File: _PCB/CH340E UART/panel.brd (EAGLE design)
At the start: 21.1 x 11.4 mm, 11 parts, among them IC1 REG1117

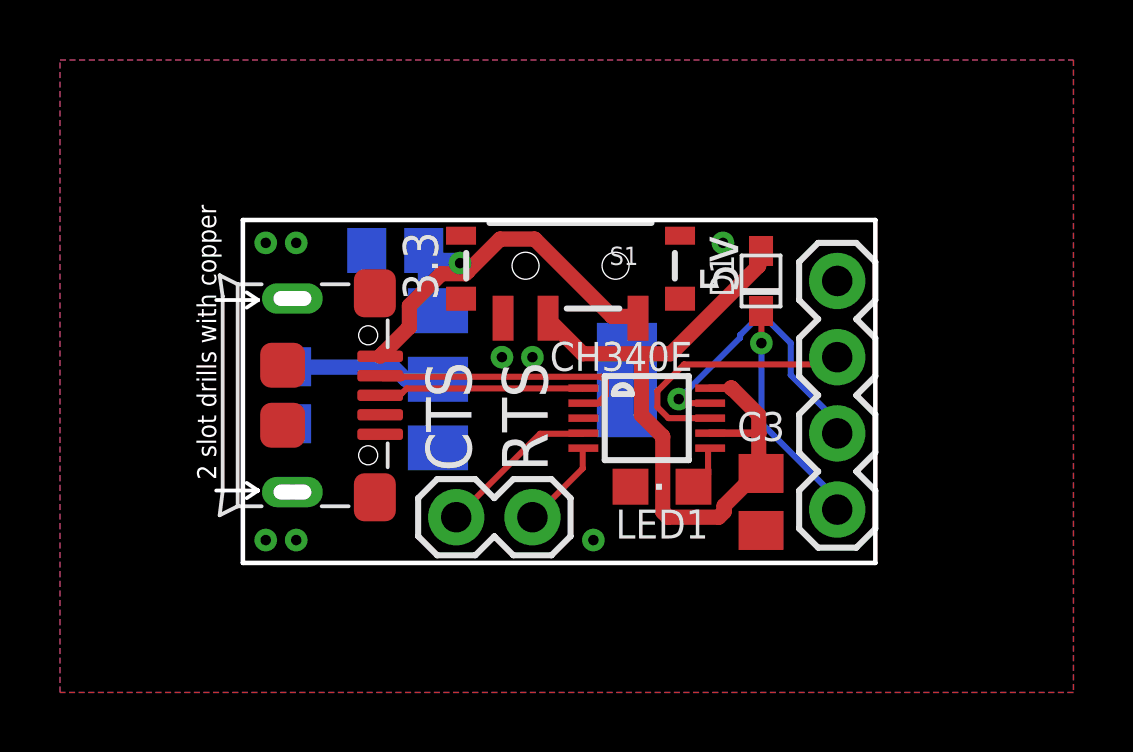
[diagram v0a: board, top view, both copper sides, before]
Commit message: CH340E converter complete + LoRa sensor node
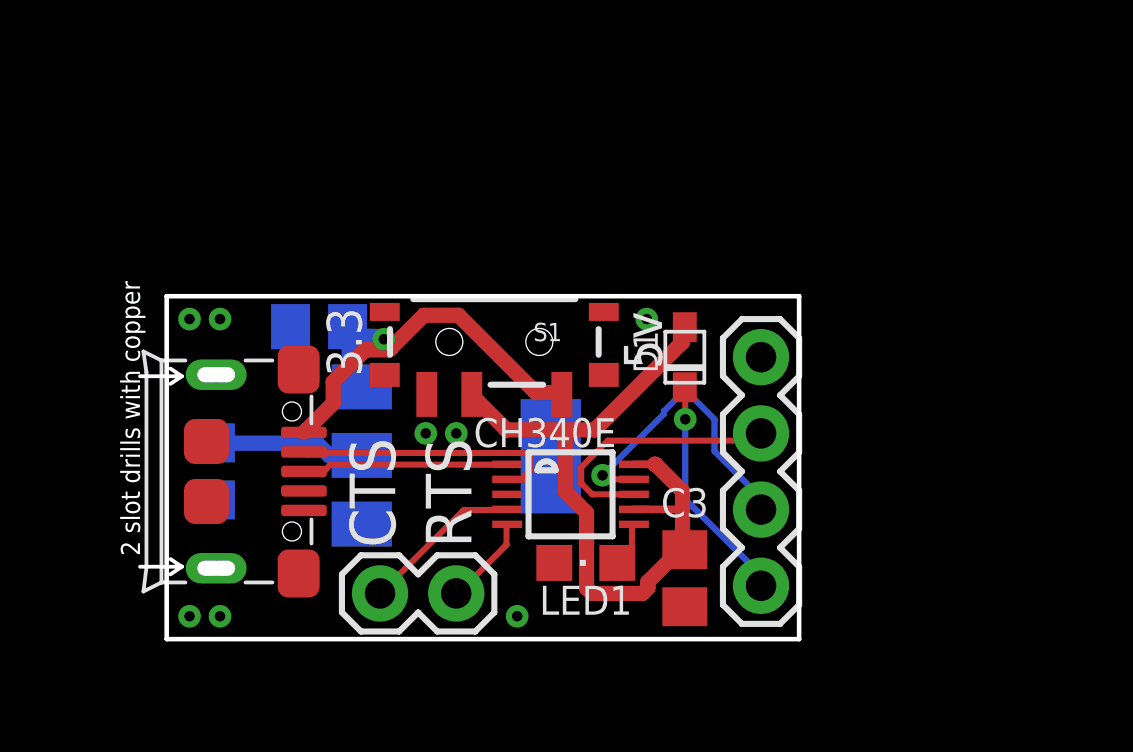
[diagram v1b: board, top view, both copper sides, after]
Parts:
- moved D1 3.59 mm to (17.3, 9.40)
- moved C3 3.59 mm to (17.3, 2.03)
- moved C1 3.59 mm to (5.08, 10.4)
- moved J2 3.59 mm to (9.65, 1.52)
- moved LED1 3.59 mm to (14.0, 2.54)
- moved C2 3.59 mm to (1.52, 5.59)
- moved USB2 3.59 mm to (4.83, 5.59)
- moved CH340E 3.59 mm to (13.5, 4.83)
- moved IC1 3.59 mm to (9.65, 6.10)
- moved J1 3.59 mm to (19.8, 1.78)
- moved S1 3.59 mm to (10.9, 9.91)
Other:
- board text added: "C1"
- board text added: "C2"
- board text added: "C3"
- board text added: "CH340E"
- board text added: "D1"
- board text added: "LED1"
- board text added: "S1"

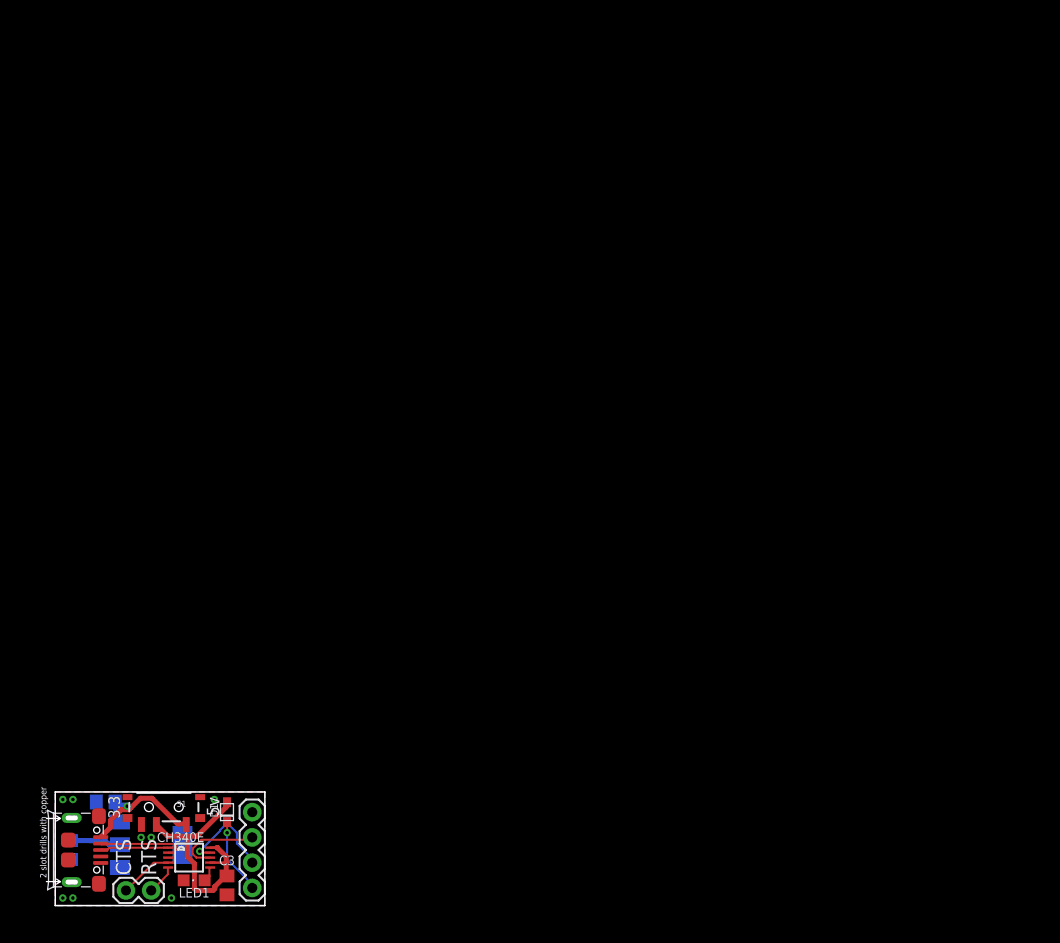
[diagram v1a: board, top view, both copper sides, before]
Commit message: CH340E board panelized
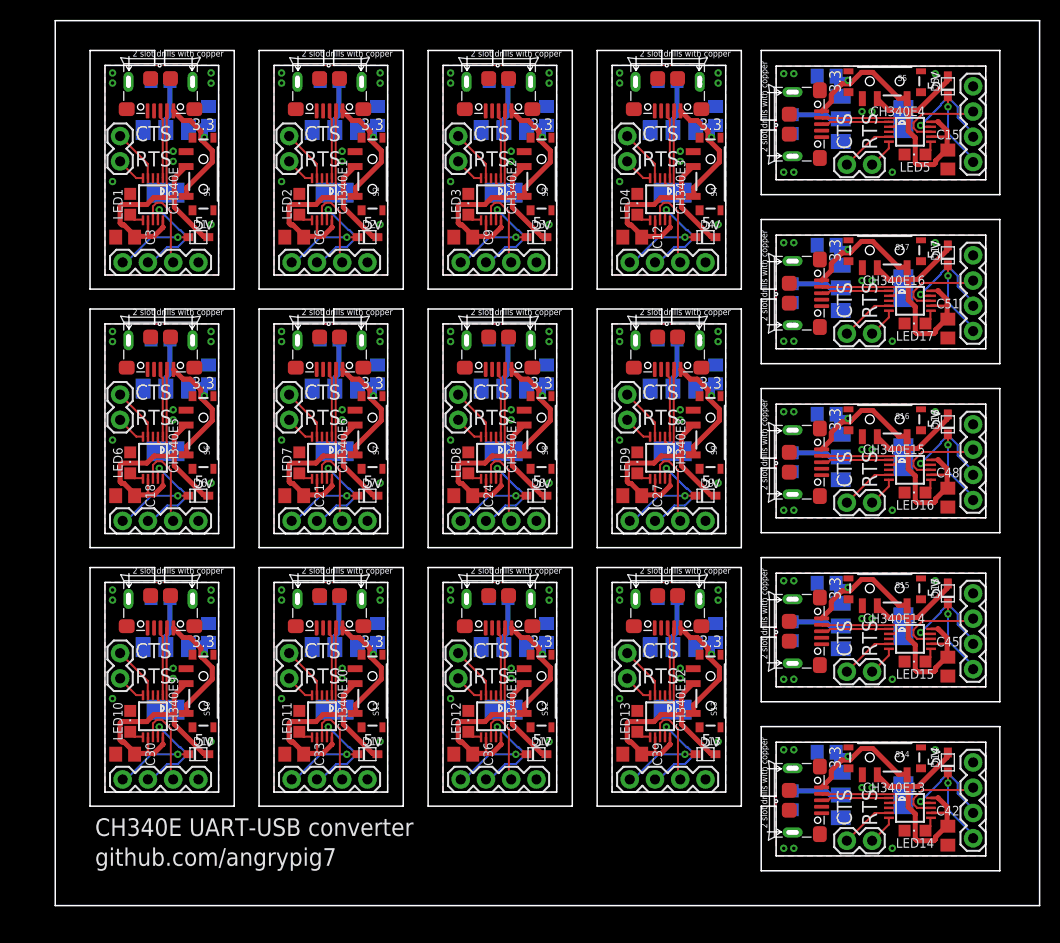
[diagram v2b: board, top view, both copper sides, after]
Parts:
- added C10, C11, C12, C13, C14, C15, C16, C17, C18, C19, C20, C21, C22, C23, C24, C25, C26, C27, C28, C29, C30, C31, C32, C33, C34, C35, C36, C37, C38, C39, C4, C40, C41, C42, C43, C44, C45, C46, C47, C48, C49, C5, C50, C51, C6, C7, C8, C9: 100nF, rcl-2:C0805
- added CH340E1, CH340E10, CH340E11, CH340E12, CH340E13, CH340E14, CH340E15, CH340E16, CH340E2, CH340E3, CH340E4, CH340E5, CH340E6, CH340E7, CH340E8, CH340E9: CH340ESMD, CH340E:MSOP10
- added D10, D11, D12, D13, D14, D15, D16, D17, D2, D3, D4, D5, D6, D7, D8, D9: (no value), adafruit:SOD-323F
- added IC10, IC11, IC12, IC13, IC14, IC15, IC16, IC17, IC2, IC3, IC4, IC5, IC6, IC7, IC8, IC9: REG1117, burr-brown-3:SOT223
- added J10, J12, J14, J16, J18, J20, J22, J24, J26, J28, J30, J32, J34, J4, J6, J8: (no value), SparkFun-Connectors:1X02
- added J11, J13, J15, J17, J19, J21, J23, J25, J27, J29, J3, J31, J33, J5, J7, J9: (no value), SparkFun-Connectors:1X04
- added LED10, LED11, LED12, LED13, LED14, LED15, LED16, LED17, LED2, LED3, LED4, LED5, LED6, LED7, LED8, LED9: (no value), adafruit:CHIPLED_0805
- added S10, S11, S12, S13, S14, S15, S16, S17, S2, S3, S4, S5, S6, S7, S8, S9: (no value), SparkFun-Switches:SWITCH_SPST_SMD_A
- added USB1, USB10, USB11, USB12, USB13, USB14, USB15, USB16, USB17, USB3, USB4, USB5, USB6, USB7, USB8, USB9: ST-USB-001G, Seeed-Connector:MICRO-USB5+4P-SMD-0.65-B
- moved C2 77.9 mm to (10.6, 83.0), turned to 0 degrees
- moved USB2 74.3 mm to (10.6, 79.7), turned to 180 degrees
- moved J2 73.4 mm to (6.52, 74.8), turned to 90 degrees
- moved C1 69.8 mm to (15.4, 79.4), turned to 90 degrees
- moved IC1 68.8 mm to (11.1, 74.8), turned to 180 degrees
- moved LED1 68.3 mm to (7.54, 70.5), turned to 0 degrees
- moved CH340E 66.3 mm to (9.83, 71.0), turned to 270 degrees
- moved C3 66.0 mm to (7.03, 67.2), turned to 180 degrees
- moved J1 64.2 mm to (6.78, 64.7), turned to 0 degrees
- moved S1 63.8 mm to (14.9, 73.6), turned to 270 degrees
- moved D1 57.9 mm to (14.4, 67.2), turned to 180 degrees
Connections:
- new net 3.3V1: S2.1
- new net 3.3V10: S11.1
- new net 3.3V11: S12.1
- new net 3.3V12: S13.1
- new net 3.3V13: S14.1
- new net 3.3V14: S15.1
- new net 3.3V15: S16.1
- new net 3.3V16: S17.1
- new net 3.3V2: S3.1
- new net 3.3V3: S4.1
- new net 3.3V4: S5.1
- new net 3.3V5: S6.1
- new net 3.3V6: S7.1
- new net 3.3V7: S8.1
- new net 3.3V8: S9.1
- new net 3.3V9: S10.1
- new net 3V1: C5.1, IC2.2
- new net 3V10: C29.1, IC10.2
- new net 3V11: C32.1, IC11.2
- new net 3V12: C35.1, IC12.2
- new net 3V13: C38.1, IC13.2
- new net 3V14: C41.1, IC14.2
- new net 3V15: C44.1, IC15.2
- new net 3V16: C47.1, IC16.2
- new net 3V17: C50.1, IC17.2
- new net 3V2: C8.1, IC3.2
- new net 3V4: C11.1, IC4.2
- new net 3V5: C14.1, IC5.2
- new net 3V6: C17.1, IC6.2
- new net 3V7: C20.1, IC7.2
- new net 3V8: C23.1, IC8.2
- new net 3V9: C26.1, IC9.2
- new net 5V1: C4.1, IC2.3, S2.3, USB1.1
- new net 5V10: C31.1, IC11.3, S11.3, USB11.1
- new net 5V11: C34.1, IC12.3, S12.3, USB12.1
- new net 5V12: C37.1, IC13.3, S13.3, USB13.1
- new net 5V13: C40.1, IC14.3, S14.3, USB14.1
- new net 5V14: C43.1, IC15.3, S15.3, USB15.1
- new net 5V15: C46.1, IC16.3, S16.3, USB16.1
- new net 5V16: C49.1, IC17.3, S17.3, USB17.1
- new net 5V2: C7.1, IC3.3, S3.3, USB3.1
- new net 5V3: C10.1, IC4.3, S4.3, USB4.1
- new net 5V4: C13.1, IC5.3, S5.3, USB5.1
- new net 5V5: C16.1, IC6.3, S6.3, USB6.1
- new net 5V6: C19.1, IC7.3, S7.3, USB7.1
- new net 5V7: C22.1, IC8.3, S8.3, USB8.1
- new net 5V8: C25.1, IC9.3, S9.3, USB9.1
- new net 5V9: C28.1, IC10.3, S10.3, USB10.1
- new net CTS1: CH340E1.5, J4.1
- new net CTS10: CH340E10.5, J22.1
- new net CTS11: CH340E11.5, J24.1
- new net CTS12: CH340E12.5, J26.1
- new net CTS13: CH340E13.5, J28.1
- new net CTS14: CH340E14.5, J30.1
- new net CTS15: CH340E15.5, J32.1
- new net CTS16: CH340E16.5, J34.1
- new net CTS2: CH340E2.5, J6.1
- new net CTS3: CH340E3.5, J8.1
- new net CTS4: CH340E4.5, J10.1
- new net CTS5: CH340E5.5, J12.1
- new net CTS6: CH340E6.5, J14.1
- new net CTS7: CH340E7.5, J16.1
- new net CTS8: CH340E8.5, J18.1
- new net CTS9: CH340E9.5, J20.1
- new net GND1: C4.2, C5.2, C6.2, CH340E1.3, IC2.1, J3.4, LED2.C, USB1.5, USB1.S1, USB1.S2, USB1.S3, USB1.S4, USB1.S5, USB1.S6
- new net GND10: C31.2, C32.2, C33.2, CH340E10.3, IC11.1, J21.4, LED11.C, USB11.5, USB11.S1, USB11.S2, USB11.S3, USB11.S4, USB11.S5, USB11.S6
- new net GND11: C34.2, C35.2, C36.2, CH340E11.3, IC12.1, J23.4, LED12.C, USB12.5, USB12.S1, USB12.S2, USB12.S3, USB12.S4, USB12.S5, USB12.S6
- new net GND12: C37.2, C38.2, C39.2, CH340E12.3, IC13.1, J25.4, LED13.C, USB13.5, USB13.S1, USB13.S2, USB13.S3, USB13.S4, USB13.S5, USB13.S6
- new net GND13: C40.2, C41.2, C42.2, CH340E13.3, IC14.1, J27.4, LED14.C, USB14.5, USB14.S1, USB14.S2, USB14.S3, USB14.S4, USB14.S5, USB14.S6
- new net GND14: C43.2, C44.2, C45.2, CH340E14.3, IC15.1, J29.4, LED15.C, USB15.5, USB15.S1, USB15.S2, USB15.S3, USB15.S4, USB15.S5, USB15.S6
- new net GND15: C46.2, C47.2, C48.2, CH340E15.3, IC16.1, J31.4, LED16.C, USB16.5, USB16.S1, USB16.S2, USB16.S3, USB16.S4, USB16.S5, USB16.S6
- new net GND16: C49.2, C50.2, C51.2, CH340E16.3, IC17.1, J33.4, LED17.C, USB17.5, USB17.S1, USB17.S2, USB17.S3, USB17.S4, USB17.S5, USB17.S6
- new net GND2: C7.2, C8.2, C9.2, CH340E2.3, IC3.1, J5.4, LED3.C, USB3.5, USB3.S1, USB3.S2, USB3.S3, USB3.S4, USB3.S5, USB3.S6
- new net GND3: C10.2, C11.2, C12.2, CH340E3.3, IC4.1, J7.4, LED4.C, USB4.5, USB4.S1, USB4.S2, USB4.S3, USB4.S4, USB4.S5, USB4.S6
- new net GND4: C13.2, C14.2, C15.2, CH340E4.3, IC5.1, J9.4, LED5.C, USB5.5, USB5.S1, USB5.S2, USB5.S3, USB5.S4, USB5.S5, USB5.S6
- new net GND5: C16.2, C17.2, C18.2, CH340E5.3, IC6.1, J11.4, LED6.C, USB6.5, USB6.S1, USB6.S2, USB6.S3, USB6.S4, USB6.S5, USB6.S6
- new net GND6: C19.2, C20.2, C21.2, CH340E6.3, IC7.1, J13.4, LED7.C, USB7.5, USB7.S1, USB7.S2, USB7.S3, USB7.S4, USB7.S5, USB7.S6
- new net GND7: C22.2, C23.2, C24.2, CH340E7.3, IC8.1, J15.4, LED8.C, USB8.5, USB8.S1, USB8.S2, USB8.S3, USB8.S4, USB8.S5, USB8.S6
- new net GND8: C25.2, C26.2, C27.2, CH340E8.3, IC9.1, J17.4, LED9.C, USB9.5, USB9.S1, USB9.S2, USB9.S3, USB9.S4, USB9.S5, USB9.S6
- new net GND9: C28.2, C29.2, C30.2, CH340E9.3, IC10.1, J19.4, LED10.C, USB10.5, USB10.S1, USB10.S2, USB10.S3, USB10.S4, USB10.S5, USB10.S6
- new net N$10: CH340E9.6, LED10.A
- new net N$11: CH340E10.6, LED11.A
- new net N$12: CH340E11.6, LED12.A
- new net N$13: CH340E12.6, LED13.A
- new net N$14: CH340E13.6, LED14.A
- new net N$15: CH340E14.6, LED15.A
- new net N$16: CH340E15.6, LED16.A
- new net N$17: CH340E16.6, LED17.A
- new net N$2: CH340E1.6, LED2.A
- new net N$3: CH340E2.6, LED3.A
- new net N$4: CH340E3.6, LED4.A
- new net N$5: CH340E4.6, LED5.A
- new net N$6: CH340E5.6, LED6.A
- new net N$7: CH340E6.6, LED7.A
- new net N$8: CH340E7.6, LED8.A
- new net N$9: CH340E8.6, LED9.A
- new net RTS1: CH340E1.4, J4.2
- new net RTS10: CH340E10.4, J22.2
- new net RTS11: CH340E11.4, J24.2
- new net RTS12: CH340E12.4, J26.2
- new net RTS13: CH340E13.4, J28.2
- new net RTS14: CH340E14.4, J30.2
- new net RTS15: CH340E15.4, J32.2
- new net RTS16: CH340E16.4, J34.2
- new net RTS2: CH340E2.4, J6.2
- new net RTS3: CH340E3.4, J8.2
- new net RTS4: CH340E4.4, J10.2
- new net RTS5: CH340E5.4, J12.2
- new net RTS6: CH340E6.4, J14.2
- new net RTS7: CH340E7.4, J16.2
- new net RTS8: CH340E8.4, J18.2
- new net RTS9: CH340E9.4, J20.2
- new net RX1: CH340E1.9, J3.2
- new net RX10: CH340E10.9, J21.2
- new net RX11: CH340E11.9, J23.2
- new net RX12: CH340E12.9, J25.2
- new net RX13: CH340E13.9, J27.2
- new net RX14: CH340E14.9, J29.2
- new net RX15: CH340E15.9, J31.2
- new net RX16: CH340E16.9, J33.2
- new net RX2: CH340E2.9, J5.2
- new net RX3: CH340E3.9, J7.2
- new net RX4: CH340E4.9, J9.2
- new net RX5: CH340E5.9, J11.2
- new net RX6: CH340E6.9, J13.2
- new net RX7: CH340E7.9, J15.2
- new net RX8: CH340E8.9, J17.2
- new net RX9: CH340E9.9, J19.2
- new net TX1: CH340E1.8, J3.3
- new net TX10: CH340E10.8, J21.3
- new net TX11: CH340E11.8, J23.3
- new net TX12: CH340E12.8, J25.3
- new net TX13: CH340E13.8, J27.3
- new net TX14: CH340E14.8, J29.3
- new net TX15: CH340E15.8, J31.3
- new net TX16: CH340E16.8, J33.3
- new net TX2: CH340E2.8, J5.3
- new net TX3: CH340E3.8, J7.3
- new net TX4: CH340E4.8, J9.3
- new net TX5: CH340E5.8, J11.3
- new net TX6: CH340E6.8, J13.3
- new net TX7: CH340E7.8, J15.3
- new net TX8: CH340E8.8, J17.3
- new net TX9: CH340E9.8, J19.3
- new net USBN1: CH340E1.2, USB1.2
- new net USBN10: CH340E10.2, USB11.2
- new net USBN11: CH340E11.2, USB12.2
- new net USBN12: CH340E12.2, USB13.2
- new net USBN13: CH340E13.2, USB14.2
- new net USBN14: CH340E14.2, USB15.2
- new net USBN15: CH340E15.2, USB16.2
- new net USBN16: CH340E16.2, USB17.2
- new net USBN2: CH340E2.2, USB3.2
- new net USBN3: CH340E3.2, USB4.2
- new net USBN4: CH340E4.2, USB5.2
- new net USBN5: CH340E5.2, USB6.2
- new net USBN6: CH340E6.2, USB7.2
- new net USBN7: CH340E7.2, USB8.2
- new net USBN8: CH340E8.2, USB9.2
- new net USBN9: CH340E9.2, USB10.2
- new net USBP1: CH340E1.1, USB1.3
- new net USBP10: CH340E10.1, USB11.3
- new net USBP11: CH340E11.1, USB12.3
- new net USBP12: CH340E12.1, USB13.3
- new net USBP13: CH340E13.1, USB14.3
- new net USBP14: CH340E14.1, USB15.3
- new net USBP15: CH340E15.1, USB16.3
- new net USBP16: CH340E16.1, USB17.3
- new net USBP2: CH340E2.1, USB3.3
- new net USBP3: CH340E3.1, USB4.3
- new net USBP4: CH340E4.1, USB5.3
- new net USBP5: CH340E5.1, USB6.3
- new net USBP6: CH340E6.1, USB7.3
- new net USBP7: CH340E7.1, USB8.3
- new net USBP8: CH340E8.1, USB9.3
- new net USBP9: CH340E9.1, USB10.3
- new net VCC1: C6.1, CH340E1.10, CH340E1.7, D2.A, S2.2
- new net VCC10: C33.1, CH340E10.10, CH340E10.7, D11.A, S11.2
- new net VCC11: C36.1, CH340E11.10, CH340E11.7, D12.A, S12.2
- new net VCC12: C39.1, CH340E12.10, CH340E12.7, D13.A, S13.2
- new net VCC13: C42.1, CH340E13.10, CH340E13.7, D14.A, S14.2
- new net VCC14: C45.1, CH340E14.10, CH340E14.7, D15.A, S15.2
- new net VCC15: C48.1, CH340E15.10, CH340E15.7, D16.A, S16.2
- new net VCC16: C51.1, CH340E16.10, CH340E16.7, D17.A, S17.2
- new net VCC2: C9.1, CH340E2.10, CH340E2.7, D3.A, S3.2
- new net VCC3: C12.1, CH340E3.10, CH340E3.7, D4.A, S4.2
- new net VCC4: C15.1, CH340E4.10, CH340E4.7, D5.A, S5.2
- new net VCC5: C18.1, CH340E5.10, CH340E5.7, D6.A, S6.2
- new net VCC6: C21.1, CH340E6.10, CH340E6.7, D7.A, S7.2
- new net VCC7: C24.1, CH340E7.10, CH340E7.7, D8.A, S8.2
- new net VCC8: C27.1, CH340E8.10, CH340E8.7, D9.A, S9.2
- new net VCC9: C30.1, CH340E9.10, CH340E9.7, D10.A, S10.2
- new net VCC_D1: D2.C, J3.1
- new net VCC_D10: D11.C, J21.1
- new net VCC_D11: D12.C, J23.1
- new net VCC_D12: D13.C, J25.1
- new net VCC_D13: D14.C, J27.1
- new net VCC_D14: D15.C, J29.1
- new net VCC_D15: D16.C, J31.1
- new net VCC_D16: D17.C, J33.1
- new net VCC_D2: D3.C, J5.1
- new net VCC_D3: D4.C, J7.1
- new net VCC_D4: D5.C, J9.1
- new net VCC_D5: D6.C, J11.1
- new net VCC_D6: D7.C, J13.1
- new net VCC_D7: D8.C, J15.1
- new net VCC_D8: D9.C, J17.1
- new net VCC_D9: D10.C, J19.1
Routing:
- net VCC16: track 0.00 -> 24.4 mm
- net VCC15: track 0.00 -> 24.4 mm
- net VCC14: track 0.00 -> 24.4 mm
- net VCC13: track 0.00 -> 24.4 mm
- net VCC4: track 0.00 -> 24.4 mm
- net VCC2: track 0.00 -> 24.4 mm
- net VCC1: track 0.00 -> 24.4 mm
- net VCC3: track 0.00 -> 24.4 mm
- net VCC11: track 0.00 -> 24.4 mm
- net VCC7: track 0.00 -> 24.4 mm
- net VCC12: track 0.00 -> 24.4 mm
- net VCC10: track 0.00 -> 24.4 mm
- net VCC9: track 0.00 -> 24.4 mm
- net VCC8: track 0.00 -> 24.4 mm
- net VCC6: track 0.00 -> 24.4 mm
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- added copper zone on layer 1, net GND1
- added copper zone on layer 16, net GND1
- added copper zone on layer 1, net GND10
- added copper zone on layer 16, net GND10
- added copper zone on layer 1, net GND11
- added copper zone on layer 16, net GND11
- added copper zone on layer 1, net GND12
- added copper zone on layer 16, net GND12
- added copper zone on layer 1, net GND13
- added copper zone on layer 16, net GND13
- added copper zone on layer 1, net GND14
- added copper zone on layer 16, net GND14
- added copper zone on layer 1, net GND15
- added copper zone on layer 16, net GND15
- added copper zone on layer 1, net GND16
- added copper zone on layer 16, net GND16
- added copper zone on layer 1, net GND2
- added copper zone on layer 16, net GND2
- added copper zone on layer 1, net GND3
- added copper zone on layer 16, net GND3
- added copper zone on layer 1, net GND4
- added copper zone on layer 16, net GND4
- added copper zone on layer 1, net GND5
- added copper zone on layer 16, net GND5
- added copper zone on layer 1, net GND6
- added copper zone on layer 16, net GND6
- added copper zone on layer 1, net GND7
- added copper zone on layer 16, net GND7
- added copper zone on layer 1, net GND8
- added copper zone on layer 16, net GND8
- added copper zone on layer 1, net GND9
- added copper zone on layer 16, net GND9
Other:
- board size 21.1 x 11.4 mm -> 99 x 89 mm
- board text added: "CH340E UART-USB converter"
- board text added: "github.com/angrypig7"
